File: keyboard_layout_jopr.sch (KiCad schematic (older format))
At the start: 228 parts, among them SW1 SW_Push, U1 ATmega32U4-AU, Y1 16MHz

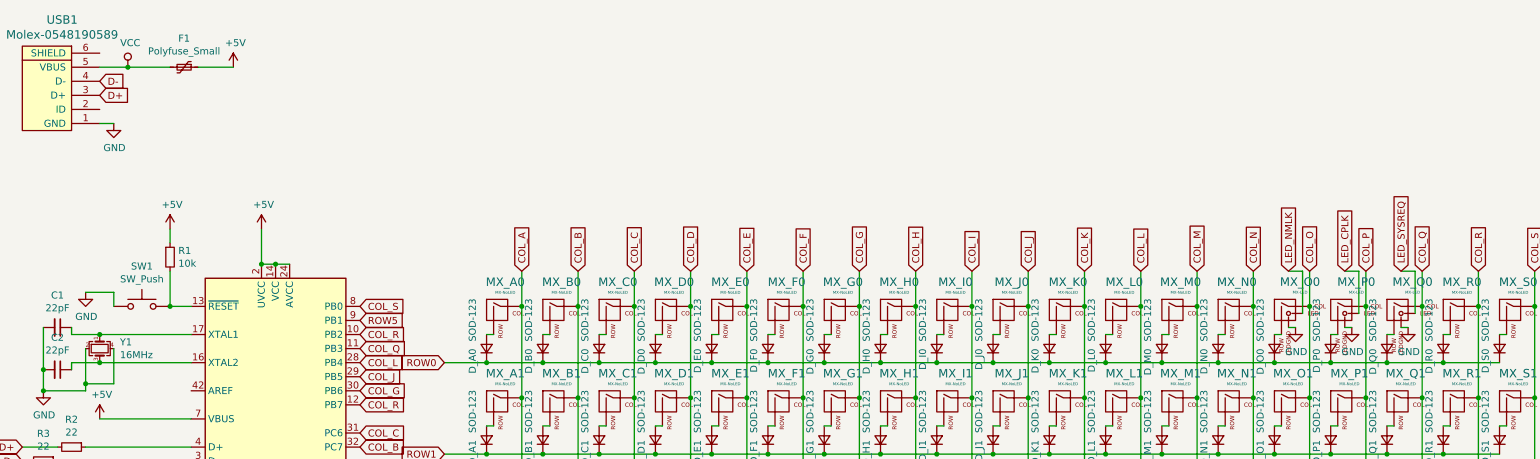
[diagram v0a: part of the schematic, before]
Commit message: added ESD-protection
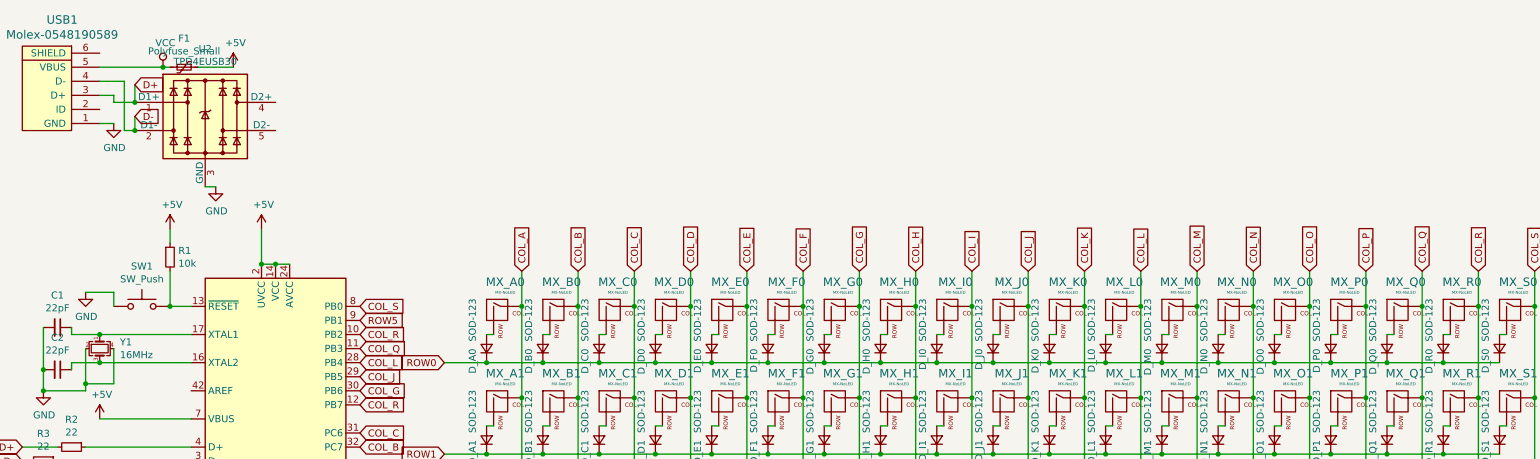
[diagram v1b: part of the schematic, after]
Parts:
- removed MX_O0, MX_P0, MX_Q0: MX-LED, MX_Only:MXOnly-1U, symbol keyboard_layout_jopr-rescue:MX-LED-MX_Alps_Hybrid
- added MX_O0, MX_P0, MX_Q0: MX-NoLED, MX_Only:MXOnly-1U-NoLED, symbol keyboard_layout_jopr-rescue:MX-NoLED-MX_Alps_Hybrid
- added U2: TPD4EUSB30, SOT65P210X110-6N:SOT65P210X110-6N, symbol Power_Protection:TPD4EUSB30
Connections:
- net COL_O: now also MX_O0.1 (COL)
- net COL_P: now also MX_P0.1 (COL)
- net COL_Q: now also MX_Q0.1 (COL)
- net D+: now also U2.1 (D1+)
- net D-: now also U2.2 (D1-)
- net GND: now also U2.3 (GND), U2.8 (GND)
- net at D_Q0.2 (A): now also MX_Q0.2 (ROW)
- net at D_P0.2 (A): now also MX_P0.2 (ROW)
- net at D_O0.2 (A): now also MX_O0.2 (ROW)
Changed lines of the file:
@@
 L power:VCC #PWR01
 U 1 1 5CFCA327
-P 1500 1000
-F 0 "#PWR01" H 1500 850 50  0001 C CNN
-F 1 "VCC" H 1517 1173 50  0000 C CNN
-F 2 "" H 1500 1000 50  0001 C CNN
-F 3 "" H 1500 1000 50  0001 C CNN
-	1    1500 1000
+P 1750 1000
+F 0 "#PWR01" H 1750 850 50  0001 C CNN
+F 1 "VCC" H 1767 1173 50  0000 C CNN
+F 2 "" H 1750 1000 50  0001 C CNN
+F 3 "" H 1750 1000 50  0001 C CNN
+	1    1750 1000
 	1    0    0    -1
 $EndComp
 Wire Wire Line
-	1300 1000 1500 1000
-Connection ~ 1500 1000
-Wire Wire Line
-	1500 1000 1800 1000
-Wire Wire Line
 	2000 1000 2250 1000
 $Comp
@@
 	1    0    0    -1
 $EndComp
-Text GLabel 1300 1100 2    50   Input ~ 0
+Text GLabel 1550 1350 2    50   Input ~ 0
 D-
-Text GLabel 1300 1200 2    50   Input ~ 0
+Text GLabel 1550 1125 2    50   Input ~ 0
 D+
 Wire Wire Line
@@
 $EndComp
 Wire Wire Line
-	10700 2450 10700 2700
-$Comp
-L keyboard_layout_jopr-rescue:MX-LED-MX_Alps_Hybrid MX_Q0
-U 1 1 5EF0C486
-P 10550 2750
-F 0 "MX_Q0" H 10632 2974 60  0000 C CNN
-F 1 "MX-LED" H 10632 2900 20  0000 C CNN
-F 2 "MX_Only:MXOnly-1U" H 9925 2725 60  0001 C CNN
-F 3 "" H 9925 2725 60  0001 C CNN
-	1    10550 2750
-	1    0    0    -1
-$EndComp
-Connection ~ 10700 2700
-Wire Wire Line
-	10700 2700 10700 3350
-$Comp
-L power:GND #PWR016
-U 1 1 5EF0C48E
-P 10600 2850
-F 0 "#PWR016" H 10600 2600 50  0001 C CNN
-F 1 "GND" H 10605 2677 50  0000 C CNN
-F 2 "" H 10600 2850 50  0001 C CNN
-F 3 "" H 10600 2850 50  0001 C CNN
-	1    10600 2850
-	1    0    0    -1
-$EndComp
-Wire Wire Line
-	10550 2850 10600 2850
-Wire Wire Line
 	10050 2900 10100 2900
 $Comp
@@
 	0    -1   -1   0
 $EndComp
-$Comp
-L keyboard_layout_jopr-rescue:MX-LED-MX_Alps_Hybrid MX_P0
-U 1 1 5EF0C49C
-P 10150 2750
-F 0 "MX_P0" H 10232 2974 60  0000 C CNN
-F 1 "MX-LED" H 10232 2900 20  0000 C CNN
-F 2 "MX_Only:MXOnly-1U" H 9525 2725 60  0001 C CNN
-F 3 "" H 9525 2725 60  0001 C CNN
-	1    10150 2750
-	1    0    0    -1
-$EndComp
-$Comp
-L power:GND #PWR015
-U 1 1 5EF0C4A2
-P 10200 2850
-F 0 "#PWR015" H 10200 2600 50  0001 C CNN
-F 1 "GND" H 10205 2677 50  0000 C CNN
-F 2 "" H 10200 2850 50  0001 C CNN
-F 3 "" H 10200 2850 50  0001 C CNN
-	1    10200 2850
-	1    0    0    -1
-$EndComp
-Wire Wire Line
-	10150 2850 10200 2850
 Wire Wire Line
 	8850 3100 9250 3100
@@
 	0    -1   -1   0
 $EndComp
-$Comp
-L keyboard_layout_jopr-rescue:MX-LED-MX_Alps_Hybrid MX_O0
-U 1 1 5EF0C4C2
-P 9750 2750
-F 0 "MX_O0" H 9832 2974 60  0000 C CNN
-F 1 "MX-LED" H 9832 2900 20  0000 C CNN
-F 2 "MX_Only:MXOnly-1U" H 9125 2725 60  0001 C CNN
-F 3 "" H 9125 2725 60  0001 C CNN
-	1    9750 2750
-	1    0    0    -1
-$EndComp
-$Comp
-L power:GND #PWR014
-U 1 1 5EF0C4C8
-P 9800 2850
-F 0 "#PWR014" H 9800 2600 50  0001 C CNN
-F 1 "GND" H 9805 2677 50  0000 C CNN
-F 2 "" H 9800 2850 50  0001 C CNN
-F 3 "" H 9800 2850 50  0001 C CNN
-	1    9800 2850
-	1    0    0    -1
-$EndComp
-Wire Wire Line
-	9750 2850 9800 2850
-Wire Wire Line
-	9850 2750 9850 2450
-Wire Wire Line
-	9850 2450 9750 2450
-Wire Wire Line
-	10300 2450 10300 2700
-Connection ~ 10300 2700
-Wire Wire Line
-	10300 2700 10300 3350
-Wire Wire Line
-	9900 2450 9900 2700
-Connection ~ 9900 2700
-Wire Wire Line
-	9900 2700 9900 3350
 Connection ~ 10050 3100
 Wire Wire Line
@@
 Wire Wire Line
 	9650 3100 10050 3100
-Wire Wire Line
-	10250 2750 10250 2450
-Wire Wire Line
-	10250 2450 10150 2450
-Wire Wire Line
-	10650 2750 10650 2450
-Wire Wire Line
-	10650 2450 10550 2450
-Text GLabel 9750 2450 1    50   Input ~ 0
-LED_NMLK
-Text GLabel 10150 2450 1    50   Input ~ 0
-LED_CPLK
-Text GLabel 10550 2450 1    50   Input ~ 0
-LED_SYSREQ
 $Comp
 L keyboard_layout_jopr-rescue:MX-NoLED-MX_Alps_Hybrid MX_I1
@@
 Text GLabel 3150 5100 2    50   Input ~ 0
 COL_D
+Connection ~ 1750 1000
+Wire Wire Line
+	1750 1000 1800 1000
+Wire Wire Line
+	1300 1000 1750 1000
+$Comp
+L Power_Protection:TPD4EUSB30 U2
+U 1 1 5D1EE78C
+P 2050 1350
+F 0 "U2" H 2050 1831 50  0000 C CNN
+F 1 "TPD4EUSB30" H 2050 1740 50  0000 C CNN
+F 2 "SOT65P210X110-6N:SOT65P210X110-6N" H 1100 950 50  0001 C CNN
+F 3 "http://www.ti.com/lit/ds/symlink/tpd2eusb30a.pdf" H 2050 1350 50  0001 C CNN
+	1    2050 1350
+	1    0    0    -1
+$EndComp
+Wire Wire Line
+	1300 1100 1475 1100
+Wire Wire Line
+	1475 1100 1475 1450
+Wire Wire Line
+	1475 1450 1550 1450
+Wire Wire Line
+	1300 1200 1400 1200
+Wire Wire Line
+	1400 1200 1400 1250
+Wire Wire Line
+	1400 1250 1550 1250
+Wire Wire Line
+	1550 1250 1550 1125
+Connection ~ 1550 1250
+Wire Wire Line
+	1550 1450 1550 1350
+Connection ~ 1550 1450
+$Comp
+L power:GND #PWR0101
+U 1 1 5D2AE673
+P 2125 1850
+F 0 "#PWR0101" H 2125 1600 50  0001 C CNN
+F 1 "GND" H 2130 1677 50  0000 C CNN
+F 2 "" H 2125 1850 50  0001 C CNN
+F 3 "" H 2125 1850 50  0001 C CNN
+	1    2125 1850
+	1    0    0    -1
+$EndComp
+Wire Wire Line
+	2050 1850 2125 1850
+Wire Wire Line
+	10700 2450 10700 2700
+Wire Wire Line
+	10300 2450 10300 2700
+Wire Wire Line
+	9900 2450 9900 2700
+$Comp
+L keyboard_layout_jopr-rescue:MX-NoLED-MX_Alps_Hybrid MX_O0
+U 1 1 5D2DFAA9
+P 9750 2750
+F 0 "MX_O0" H 9783 2973 60  0000 C CNN
+F 1 "MX-NoLED" H 9783 2899 20  0000 C CNN
+F 2 "MX_Only:MXOnly-1U-NoLED" H 9125 2725 60  0001 C CNN
+F 3 "" H 9125 2725 60  0001 C CNN
+	1    9750 2750
+	1    0    0    -1
+$EndComp
+Connection ~ 9900 2700
+Wire Wire Line
+	9900 2700 9900 3350
+$Comp
+L keyboard_layout_jopr-rescue:MX-NoLED-MX_Alps_Hybrid MX_P0
+U 1 1 5D2E0080
+P 10150 2750
+F 0 "MX_P0" H 10183 2973 60  0000 C CNN
+F 1 "MX-NoLED" H 10183 2899 20  0000 C CNN
+F 2 "MX_Only:MXOnly-1U-NoLED" H 9525 2725 60  0001 C CNN
+F 3 "" H 9525 2725 60  0001 C CNN
+	1    10150 2750
+	1    0    0    -1
+$EndComp
+Connection ~ 10300 2700
+Wire Wire Line
+	10300 2700 10300 3350
+$Comp
+L keyboard_layout_jopr-rescue:MX-NoLED-MX_Alps_Hybrid MX_Q0
+U 1 1 5D2E0A97
+P 10550 2750
+F 0 "MX_Q0" H 10583 2973 60  0000 C CNN
+F 1 "MX-NoLED" H 10583 2899 20  0000 C CNN
+F 2 "MX_Only:MXOnly-1U-NoLED" H 9925 2725 60  0001 C CNN
+F 3 "" H 9925 2725 60  0001 C CNN
+	1    10550 2750
+	1    0    0    -1
+$EndComp
+Connection ~ 10700 2700
+Wire Wire Line
+	10700 2700 10700 3350
 $EndSCHEMATC

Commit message: squared matrix, updated and renamed PDFs
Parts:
- removed U2: TPD4EUSB30, SOT65P210X110-6N:SOT65P210X110-6N, symbol Power_Protection:TPD4EUSB30
- added U2: SOT65P210X110, SOT65P210X110-6N:SOT65P210X110-6N, symbol Power_Protection:SOT65P210X110
- renumbered D_K0 to D_A6, D_K1 to D_A7, D_K2 to D_A8, D_K3 to D_A9, D_L0 to D_B6, D_L1 to D_B7, D_L2 to D_B8, D_L3 to D_B9, D_M0 to D_C6, D_M1 to D_C7, D_M2 to D_C8, D_M3 to D_C9, D_G5 to D_D5, D_N0 to D_D6, D_N1 to D_D7, D_N3 to D_D8, D_O0 to D_E6, D_O1 to D_E7, D_O2 to D_E8, D_O3 to D_E9, D_P0 to D_F6, D_P1 to D_F7, D_P2 to D_F8, D_P3 to D_F9, D_Q0 to D_G6, D_Q1 to D_G7, D_Q2 to D_G8, D_Q3 to D_G9, D_R0 to D_H6, D_R1 to D_H7, D_R2 to D_H8, D_R3 to D_H9, D_K5 to D_I5, D_N4 to D_I6, D_M4 to D_I7, D_L4 to D_I8, D_K4 to D_I9, D_R4 to D_J6, D_Q4 to D_J7, D_P4 to D_J8, D_O4 to D_J9, MX_K0 to MX_A6, MX_K1 to MX_A7, MX_K2 to MX_A8, MX_K3 to MX_A9, MX_L0 to MX_B6, MX_L1 to MX_B7, MX_L2 to MX_B8, MX_L3 to MX_B9, MX_M0 to MX_C6, MX_M1 to MX_C7, MX_M2 to MX_C8, MX_M3 to MX_C9, MX_G5 to MX_D5, MX_N0 to MX_D6, MX_N1 to MX_D7, MX_N3 to MX_D8, MX_M5 to MX_E5, MX_O0 to MX_E6, MX_O1 to MX_E7, MX_O2 to MX_E8, MX_O3 to MX_E9, MX_P0 to MX_F6, MX_P1 to MX_F7, MX_P2 to MX_F8, MX_P3 to MX_F9, MX_Q0 to MX_G6, MX_Q1 to MX_G7, MX_Q2 to MX_G8, MX_Q3 to MX_G9, MX_R0 to MX_H6, MX_R1 to MX_H7, MX_R2 to MX_H8, MX_R3 to MX_H9, MX_K5 to MX_I5, MX_N4 to MX_I6, MX_M4 to MX_I7, MX_L4 to MX_I8, MX_K4 to MX_I9, MX_R4 to MX_J6, MX_Q4 to MX_J7, MX_P4 to MX_J8, MX_O4 to MX_J9, MX_S0 to MX_K0, MX_S1 to MX_K1, MX_S3 to MX_K2, MX_S4 to MX_K3, MX_S5 to MX_K4, MX_R5 to MX_K5, MX_Q5 to MX_K6, MX_P5 to MX_K7, MX_N5 to MX_K8, MX_L5 to MX_K9
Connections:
- net COL_A: now also MX_A6.1 (COL), MX_A7.1 (COL), MX_A8.1 (COL), MX_A9.1 (COL), U1.11 (PB3); no longer U1.36 (PF7)
- net COL_B: now also MX_B6.1 (COL), MX_B7.1 (COL), MX_B8.1 (COL), MX_B9.1 (COL), U1.10 (PB2); no longer U1.32 (PC7)
- net COL_C: now also MX_C6.1 (COL), MX_C7.1 (COL), MX_C8.1 (COL), MX_C9.1 (COL), U1.9 (PB1); no longer U1.31 (PC6)
- net COL_D: now also MX_D5.1 (COL), MX_D6.1 (COL), MX_D7.1 (COL), MX_D8.1 (COL), U1.8 (PB0); no longer U1.41 (PF0)
- net COL_E: now also MX_E5.1 (COL), MX_E6.1 (COL), MX_E7.1 (COL), MX_E8.1 (COL), MX_E9.1 (COL), U1.36 (PF7); no longer U1.40 (PF1)
- net COL_F: now also MX_F6.1 (COL), MX_F7.1 (COL), MX_F8.1 (COL), MX_F9.1 (COL), U1.1 (PE6); no longer U1.39 (PF4)
- net COL_G: now also MX_G6.1 (COL), MX_G7.1 (COL), MX_G8.1 (COL), MX_G9.1 (COL), U1.37 (PF6); no longer MX_D5.1 (COL), U1.30 (PB6)
- net COL_H: now also MX_H6.1 (COL), MX_H7.1 (COL), MX_H8.1 (COL), MX_H9.1 (COL), U1.29 (PB5); no longer U1.38 (PF5)
- net COL_I: now also MX_I5.1 (COL), MX_I6.1 (COL), MX_I7.1 (COL), MX_I8.1 (COL), MX_I9.1 (COL), U1.32 (PC7); no longer U1.37 (PF6)
- net COL_J: now also MX_J6.1 (COL), MX_J7.1 (COL), MX_J8.1 (COL), MX_J9.1 (COL), U1.28 (PB4); no longer U1.29 (PB5)
- net COL_K: now also MX_K0.1 (COL), MX_K1.1 (COL), MX_K2.1 (COL), MX_K3.1 (COL), MX_K4.1 (COL), MX_K5.1 (COL), MX_K6.1 (COL), MX_K7.1 (COL), MX_K8.1 (COL), MX_K9.1 (COL), U1.19 (PD1); no longer MX_A6.1 (COL), MX_A7.1 (COL), MX_A8.1 (COL), MX_A9.1 (COL), MX_I5.1 (COL), MX_I9.1 (COL), U1.27 (PD7)
- net D+: now also U2.1 (D1+)
- net D-: now also U2.2 (D1-)
- net GND: now also U2.3 (GND), U2.8 (GND)
- net ROW0: now also U1.18 (PD0); no longer D_A6.1 (K), D_B6.1 (K), D_C6.1 (K), D_D6.1 (K), D_E6.1 (K), D_F6.1 (K), D_G6.1 (K), D_H6.1 (K)
- net ROW1: now also U1.26 (PD6); no longer D_A7.1 (K), D_B7.1 (K), D_C7.1 (K), D_D7.1 (K), D_E7.1 (K), D_F7.1 (K), D_G7.1 (K), D_H7.1 (K), U1.20 (PD2)
- net ROW2: now also D_S3.1 (K), U1.20 (PD2); no longer D_A8.1 (K), D_B8.1 (K), D_C8.1 (K), D_E8.1 (K), D_F8.1 (K), D_G8.1 (K), D_H8.1 (K)
- net ROW3: now also D_S4.1 (K), U1.25 (PD4); no longer D_A9.1 (K), D_B9.1 (K), D_C9.1 (K), D_D8.1 (K), D_E9.1 (K), D_F9.1 (K), D_G9.1 (K), D_H9.1 (K), D_S3.1 (K), U1.19 (PD1)
- net ROW4: now also D_S5.1 (K), U1.21 (PD3); no longer D_I6.1 (K), D_I7.1 (K), D_I8.1 (K), D_I9.1 (K), D_J6.1 (K), D_J7.1 (K), D_J8.1 (K), D_J9.1 (K), D_S4.1 (K), U1.18 (PD0)
- net ROW5: now also U1.22 (PD5); no longer D_L5.1 (K), D_N5.1 (K), D_P5.1 (K), D_Q5.1 (K), D_S5.1 (K), U1.9 (PB1)
- removed net COL_L: MX_B6.1 (COL), MX_B7.1 (COL), MX_B8.1 (COL), MX_B9.1 (COL), MX_I8.1 (COL), MX_K9.1 (COL), U1.28 (PB4)
- removed net COL_M: MX_C6.1 (COL), MX_C7.1 (COL), MX_C8.1 (COL), MX_C9.1 (COL), MX_E5.1 (COL), MX_I7.1 (COL), U1.22 (PD5)
- removed net COL_N: MX_D6.1 (COL), MX_D7.1 (COL), MX_D8.1 (COL), MX_I6.1 (COL), MX_K8.1 (COL), U1.25 (PD4)
- removed net COL_O: MX_E6.1 (COL), MX_E7.1 (COL), MX_E8.1 (COL), MX_E9.1 (COL), MX_J9.1 (COL), U1.26 (PD6)
- removed net COL_P: MX_F6.1 (COL), MX_F7.1 (COL), MX_F8.1 (COL), MX_F9.1 (COL), MX_J8.1 (COL), MX_K7.1 (COL), U1.21 (PD3)
- removed net COL_Q: MX_G6.1 (COL), MX_G7.1 (COL), MX_G8.1 (COL), MX_G9.1 (COL), MX_J7.1 (COL), MX_K6.1 (COL), U1.11 (PB3)
- removed net COL_R: MX_H6.1 (COL), MX_H7.1 (COL), MX_H8.1 (COL), MX_H9.1 (COL), MX_J6.1 (COL), MX_K5.1 (COL), U1.10 (PB2), U1.12 (PB7)
- removed net COL_S: MX_K0.1 (COL), MX_K1.1 (COL), MX_K2.1 (COL), MX_K3.1 (COL), MX_K4.1 (COL), U1.8 (PB0)
- new net ROW6: D_A6.1 (K), D_B6.1 (K), D_C6.1 (K), D_D6.1 (K), D_E6.1 (K), D_F6.1 (K), D_G6.1 (K), D_H6.1 (K), D_I6.1 (K), D_J6.1 (K), U1.27 (PD7)
- new net ROW7: D_A7.1 (K), D_B7.1 (K), D_C7.1 (K), D_D7.1 (K), D_E7.1 (K), D_F7.1 (K), D_G7.1 (K), D_H7.1 (K), D_I7.1 (K), D_J7.1 (K), D_P5.1 (K), U1.31 (PC6)
- new net ROW8: D_A8.1 (K), D_B8.1 (K), D_C8.1 (K), D_D8.1 (K), D_E8.1 (K), D_F8.1 (K), D_G8.1 (K), D_H8.1 (K), D_I8.1 (K), D_J8.1 (K), D_N5.1 (K), U1.30 (PB6)
- new net ROW9: D_A9.1 (K), D_B9.1 (K), D_C9.1 (K), D_E9.1 (K), D_F9.1 (K), D_G9.1 (K), D_H9.1 (K), D_I9.1 (K), D_J9.1 (K), D_L5.1 (K), U1.38 (PF5)
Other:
- moved on the sheet: D_A0, D_A1, D_A2, D_A3, D_A4, D_A5, D_A6, D_A7, D_A8, D_A9, D_B0, D_B1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
